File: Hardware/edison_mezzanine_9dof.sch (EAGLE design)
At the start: 37 parts, among them U1 LSM9DS0, U2 EDISON_CONNECTOR_FULLMOUNTING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, U3 EDISON_CONNECTOR_FULLHEADER

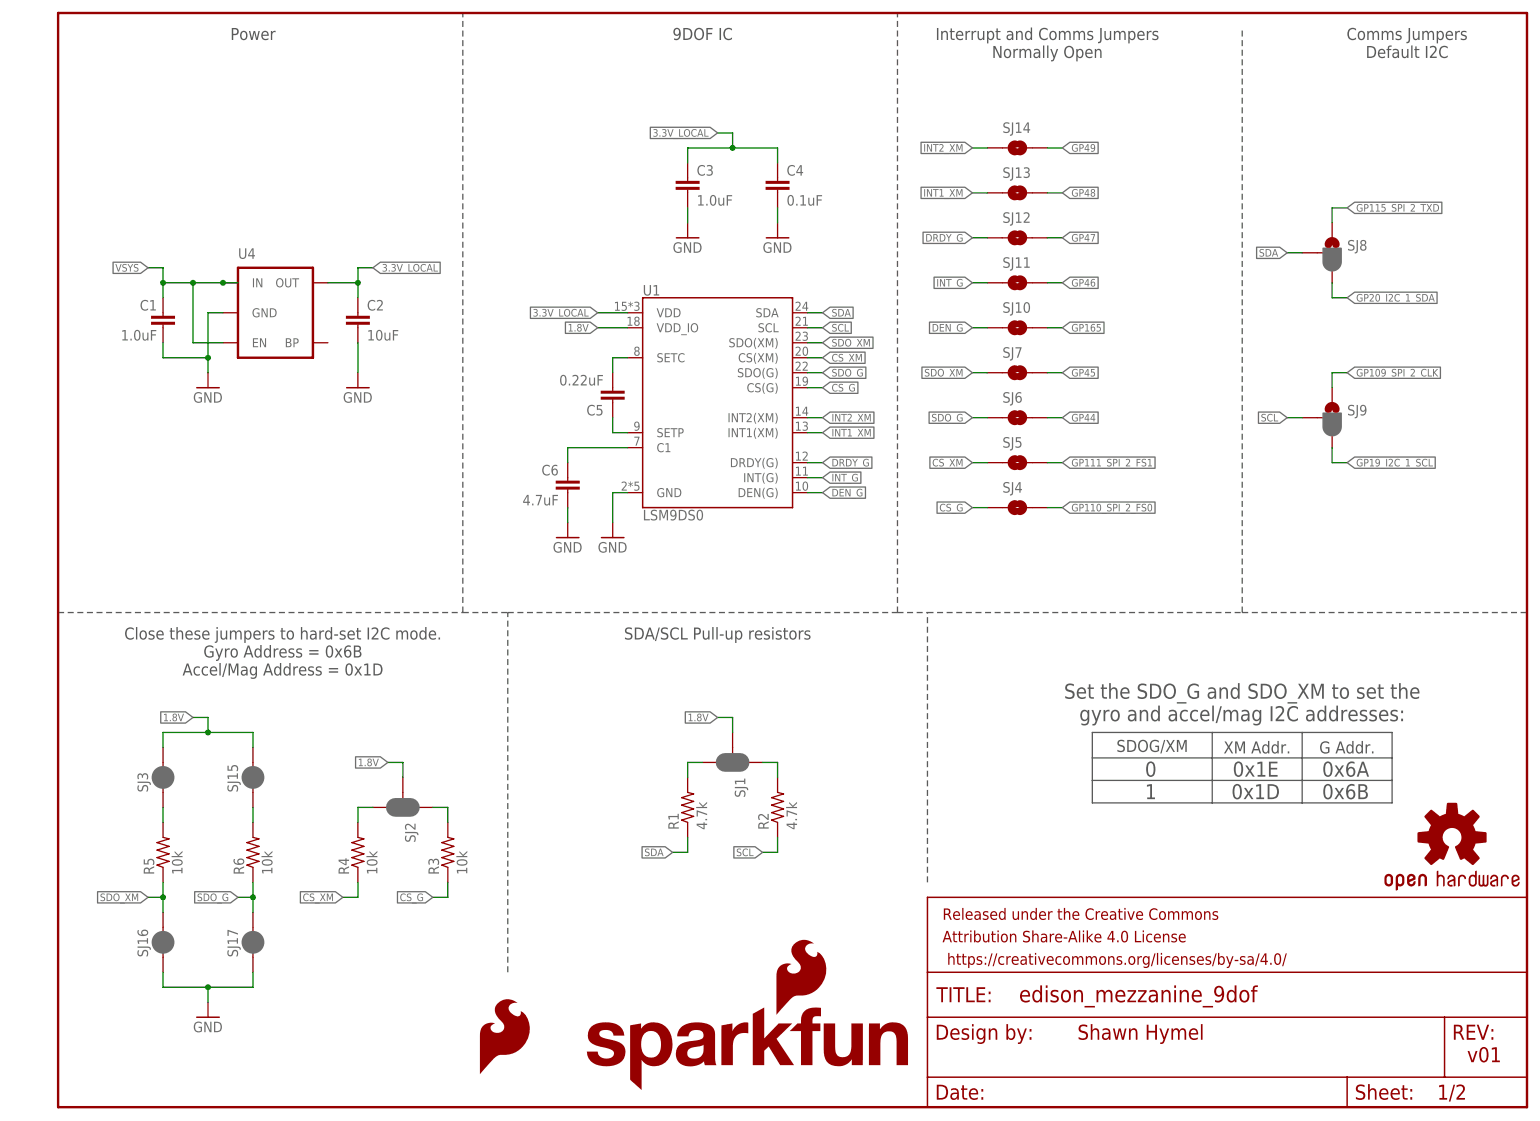
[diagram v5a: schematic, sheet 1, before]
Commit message: Added fiducials and moved ver text on layout. Moved address table near pullups/pulldowns on schematic.
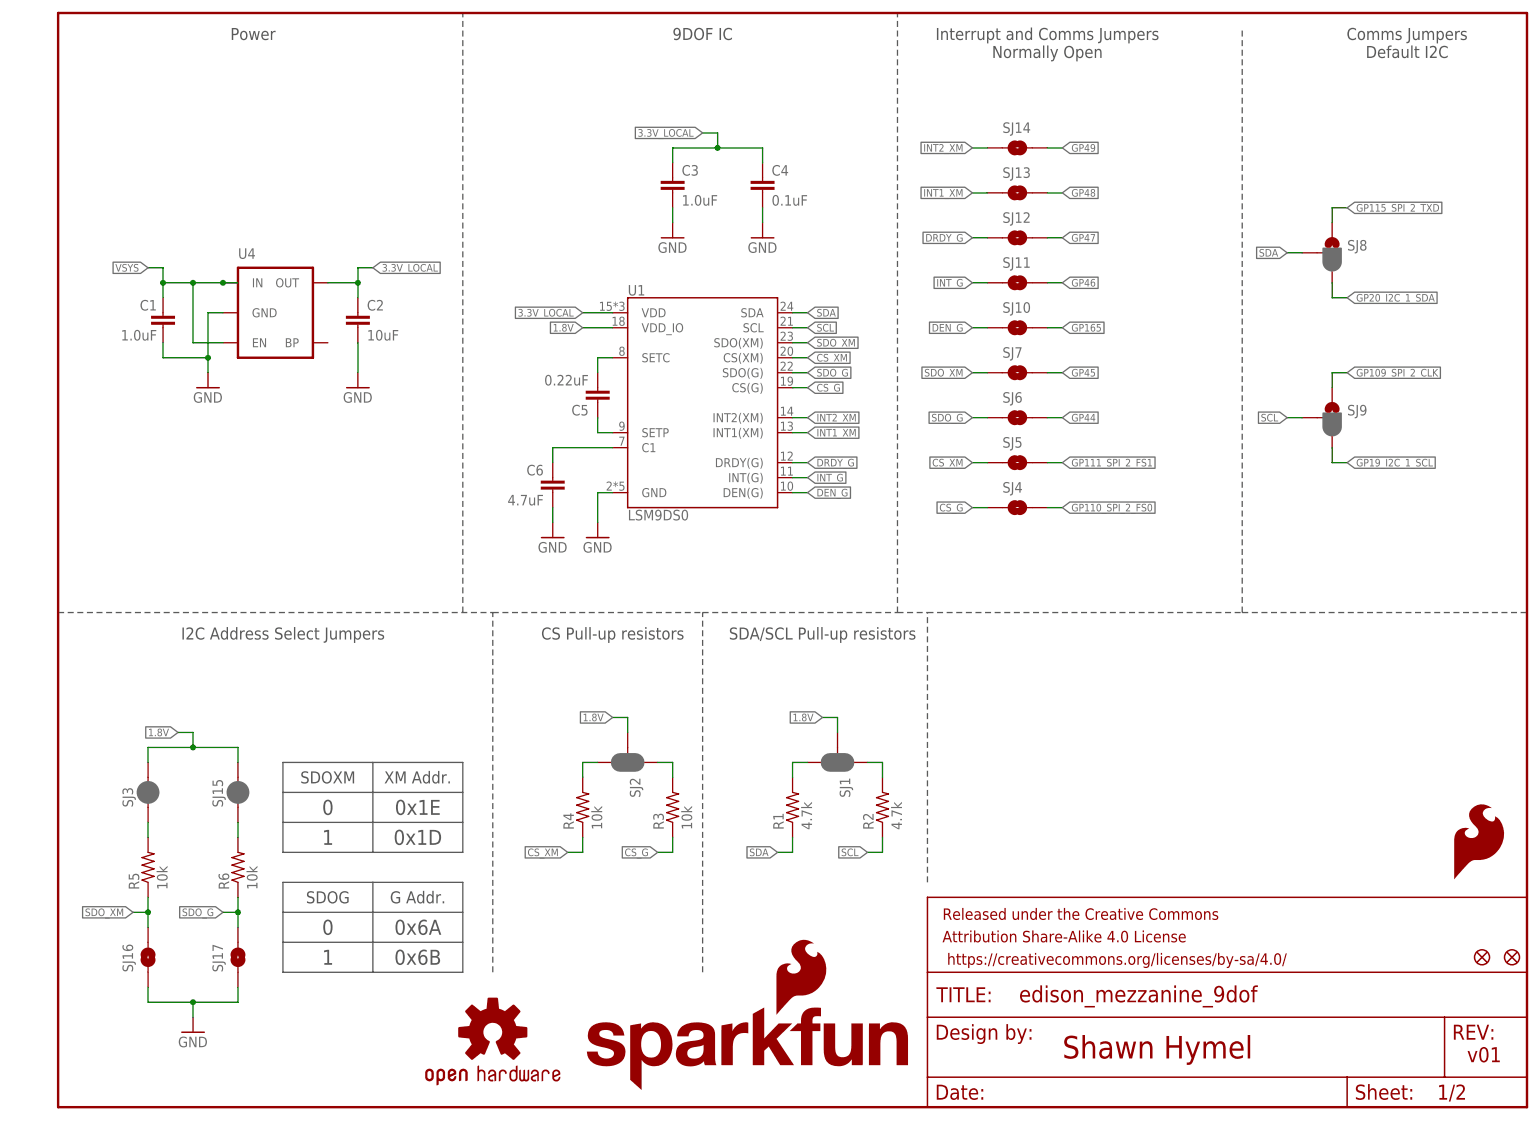
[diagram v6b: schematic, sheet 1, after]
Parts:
- added FID1, FID2: FIDUCIAL1X2, SparkFun-Aesthetics:FIDUCIAL1X2
- added FRAME2, FRAME3: FRAME-LETTER, SparkFun-Aesthetics:FRAME-LETTER
- SJ16, SJ17: value JUMPER-PAD-2-NC_BY_PASTE -> JUMPER-PAD-2-NOYES_SILK; device SparkFun-Passives:JUMPER-PAD-2-NC_BY_PASTE -> SparkFun-Passives:JUMPER-PAD-2-NOYES_SILK
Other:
- note added: "0"
- note added: "0x1D"
- note added: "0x1E"
- note added: "0x6A"
- note added: "0x6B"
- note added: "1"
- note added: "CS Pull-up resistors"
- note added: "I2C Address Select Jumpers"
- note added: "SDOG"
- note added: "SDOXM"
- note removed: "0 1"
- note removed: "0x1E 0x1D"
- note removed: "0x6A 0x6B"
- note removed: "Close these jumpers to hard-set I2C mode. Gyro Address = 0x6B Accel/Mag Address = 0x1D"
- note removed: "SDOG/XM"
- note removed: "Set the SDO_G and SDO_XM to set the gyro and accel/mag I2C addresses:"
- moved on the sheet: C3, C4, C5, C6, R1, R2, R3, R4, R5, R6, SJ1, SJ15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

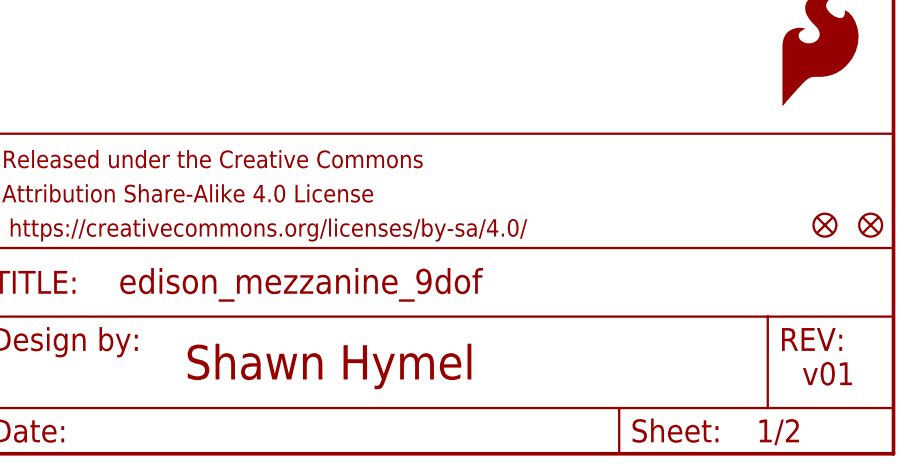
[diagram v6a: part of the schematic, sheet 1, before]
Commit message: Added second side fiducials.
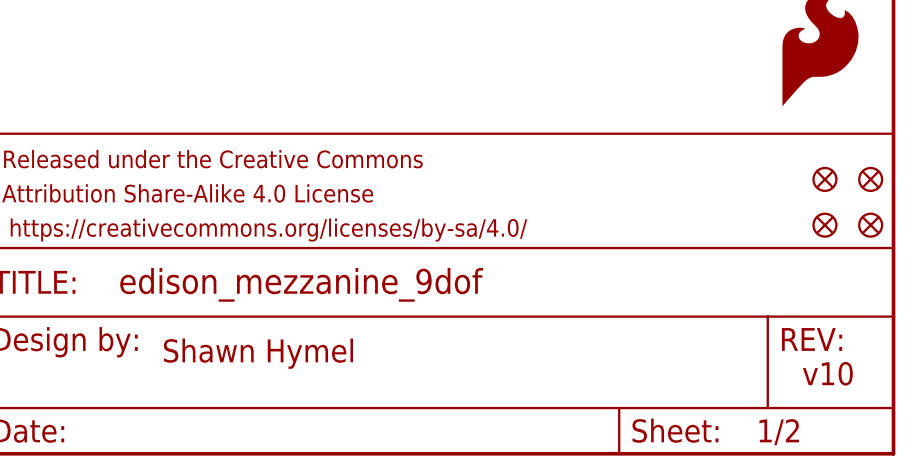
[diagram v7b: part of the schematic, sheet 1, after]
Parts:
- added FID3, FID4: FIDUCIAL1X2, SparkFun-Aesthetics:FIDUCIAL1X2
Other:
- note added: "v10"
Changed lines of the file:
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@@
 <setting verticaltext="up"/>
 </settings>
-<grid distance="0.1" unitdist="inch" unit="inch" style="lines" multiple="1" display="yes" altdistance="0.01" altunitdist="inch" altunit="inch"/>
+<grid distance="0.1" unitdist="inch" unit="inch" style="lines" multiple="1" display="no" altdistance="0.01" altunitdist="inch" altunit="inch"/>
 <layers>
 <layer number="1" name="Top" color="4" fill="1" visible="no" active="no"/>
@@
 <part name="SJ16" library="SparkFun-Passives" deviceset="JUMPER-PAD-2-NO" device="YES_SILK"/>
 <part name="SJ17" library="SparkFun-Passives" deviceset="JUMPER-PAD-2-NO" device="YES_SILK"/>
+<part name="FID3" library="SparkFun-Aesthetics" deviceset="FIDUCIAL" device="1X2"/>
+<part name="FID4" library="SparkFun-Aesthetics" deviceset="FIDUCIAL" device="1X2"/>
 </parts>
 <sheets>
@@
 <text x="228.6" y="182.88" size="2.032" layer="97" align="top-center">Comms Jumpers
 Default I2C</text>
-<text x="170.18" y="10.16" size="3.81" layer="94" align="center-left">Shawn Hymel</text>
-<text x="238.76" y="7.62" size="2.54" layer="94">v01</text>
 <wire x1="68.58" y1="83.82" x2="68.58" y2="185.42" width="0.1524" layer="97" style="longdash"/>
 <text x="33.02" y="182.88" size="2.032" layer="97" align="top-center">Power</text>
@@
 <text x="45.72" y="25.4" size="2.54" layer="97" align="center">1</text>
 <text x="60.96" y="25.4" size="2.54" layer="97" align="center">0x6B</text>
+<text x="238.76" y="7.62" size="2.54" layer="94">v10</text>
+<text x="167.64" y="10.16" size="2.54" layer="94">Shawn Hymel</text>
 </plain>
 <instances>
@@
 <attribute name="NAME" x="27.94" y="22.86" size="1.778" layer="95" rot="R90"/>
 </instance>
+<instance part="FID3" gate="G$1" x="246.38" y="30.48"/>
+<instance part="FID4" gate="G$1" x="241.3" y="30.48"/>
 </instances>
 <busses>

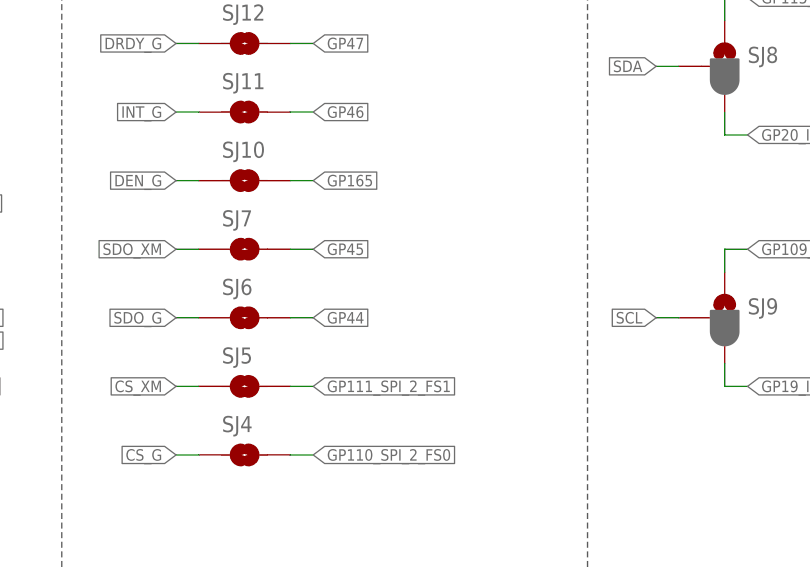
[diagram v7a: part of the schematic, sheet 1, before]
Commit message: Connected SDO_XM and SDO_G together to SPI2_RX on Edison.
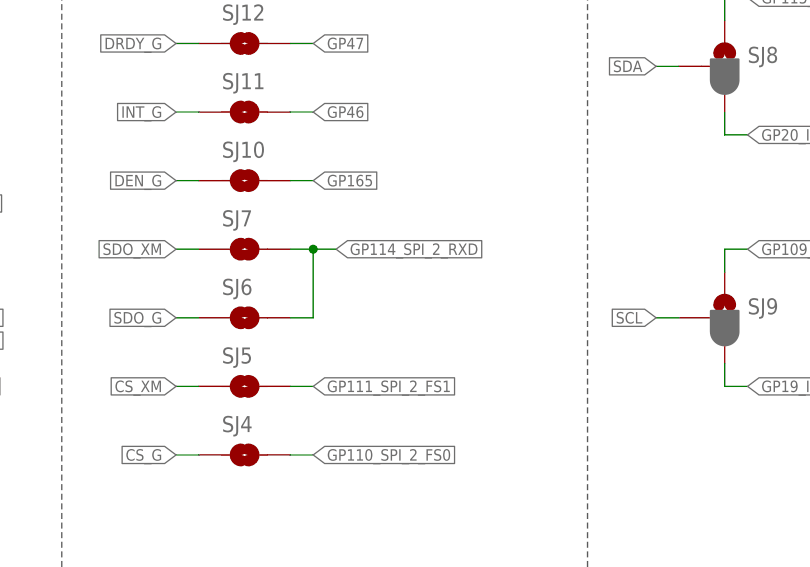
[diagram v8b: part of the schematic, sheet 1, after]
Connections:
- net GP114_SPI_2_RXD: now also SJ6.2, SJ7.2
- net GP44: no longer SJ6.2
- net GP45: no longer SJ7.2
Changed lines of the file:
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@@
 <setting verticaltext="up"/>
 </settings>
-<grid distance="0.1" unitdist="inch" unit="inch" style="lines" multiple="1" display="no" altdistance="0.01" altunitdist="inch" altunit="inch"/>
+<grid distance="0.1" unitdist="inch" unit="inch" style="lines" multiple="1" display="yes" altdistance="0.01" altunitdist="inch" altunit="inch"/>
 <layers>
 <layer number="1" name="Top" color="4" fill="1" visible="no" active="no"/>
@@
 </segment>
 </net>
-<net name="GP44" class="0">
-<segment>
-<pinref part="SJ6" gate="G$1" pin="2"/>
-<wire x1="167.64" y1="116.84" x2="170.18" y2="116.84" width="0.1524" layer="91"/>
-<label x="170.18" y="116.84" size="1.27" layer="95" xref="yes"/>
-</segment>
-</net>
-<net name="GP45" class="0">
-<segment>
-<pinref part="SJ7" gate="G$1" pin="2"/>
-<wire x1="167.64" y1="124.46" x2="170.18" y2="124.46" width="0.1524" layer="91"/>
-<label x="170.18" y="124.46" size="1.27" layer="95" xref="yes"/>
-</segment>
-</net>
 <net name="GP48" class="0">
 <segment>
@@
 </segment>
 </net>
+<net name="GP114_SPI_2_RXD" class="0">
+<segment>
+<pinref part="SJ7" gate="G$1" pin="2"/>
+<wire x1="167.64" y1="124.46" x2="170.18" y2="124.46" width="0.1524" layer="91"/>
+<wire x1="170.18" y1="124.46" x2="170.18" y2="116.84" width="0.1524" layer="91"/>
+<pinref part="SJ6" gate="G$1" pin="2"/>
+<wire x1="170.18" y1="116.84" x2="167.64" y2="116.84" width="0.1524" layer="91"/>
+<wire x1="170.18" y1="124.46" x2="172.72" y2="124.46" width="0.1524" layer="91"/>
+<junction x="170.18" y="124.46"/>
+<label x="172.72" y="124.46" size="1.27" layer="95" xref="yes"/>
+</segment>
+</net>
